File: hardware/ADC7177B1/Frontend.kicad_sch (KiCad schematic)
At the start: 55 parts, among them J4 Conn_01x01, J5 Conn_01x01, J6 Conn_01x01, J7 Conn_01x01, K1 G6SK-2F-DC5, Q6 MMBT3904, Q7 MMBT3904, U12 AD8599ARZ, U13 AD8599ARZ, U14 CPC1002N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

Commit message: PCB
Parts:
- R31, R32, R33, R34, R35, R36, R37, R38, R39, R40, R41, R42: now not fitted; now left out of the parts list
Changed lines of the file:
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@@
 		(unit 1)
 		(exclude_from_sim no)
-		(in_bom yes)
+		(in_bom no)
 		(on_board yes)
-		(dnp no)
+		(dnp yes)
 		(fields_autoplaced yes)
 		(property "Reference" "R40"
@@
 		(unit 1)
 		(exclude_from_sim no)
-		(in_bom yes)
+		(in_bom no)
 		(on_board yes)
-		(dnp no)
+		(dnp yes)
 		(fields_autoplaced yes)
 		(property "Reference" "R33"
@@
 		(unit 1)
 		(exclude_from_sim no)
-		(in_bom yes)
+		(in_bom no)
 		(on_board yes)
-		(dnp no)
+		(dnp yes)
 		(fields_autoplaced yes)
 		(property "Reference" "R38"
@@
 		(unit 1)
 		(exclude_from_sim no)
-		(in_bom yes)
+		(in_bom no)
 		(on_board yes)
-		(dnp no)
+		(dnp yes)
 		(fields_autoplaced yes)
 		(property "Reference" "R37"
@@
 		(unit 1)
 		(exclude_from_sim no)
-		(in_bom yes)
+		(in_bom no)
 		(on_board yes)
-		(dnp no)
+		(dnp yes)
 		(fields_autoplaced yes)
 		(property "Reference" "R34"
@@
 		(unit 1)
 		(exclude_from_sim no)
-		(in_bom yes)
+		(in_bom no)
 		(on_board yes)
-		(dnp no)
+		(dnp yes)
 		(fields_autoplaced yes)
 		(property "Reference" "R36"
@@
 		(unit 1)
 		(exclude_from_sim no)
-		(in_bom yes)
+		(in_bom no)
 		(on_board yes)
-		(dnp no)
+		(dnp yes)
 		(fields_autoplaced yes)
 		(property "Reference" "R31"
@@
 		(unit 1)
 		(exclude_from_sim no)
-		(in_bom yes)
+		(in_bom no)
 		(on_board yes)
-		(dnp no)
+		(dnp yes)
 		(fields_autoplaced yes)
 		(property "Reference" "R42"
@@
 		(unit 1)
 		(exclude_from_sim no)
-		(in_bom yes)
+		(in_bom no)
 		(on_board yes)
-		(dnp no)
+		(dnp yes)
 		(fields_autoplaced yes)
 		(property "Reference" "R39"
@@
 		(unit 1)
 		(exclude_from_sim no)
-		(in_bom yes)
+		(in_bom no)
 		(on_board yes)
-		(dnp no)
+		(dnp yes)
 		(fields_autoplaced yes)
 		(property "Reference" "R32"
@@
 		(unit 1)
 		(exclude_from_sim no)
-		(in_bom yes)
+		(in_bom no)
 		(on_board yes)
-		(dnp no)
+		(dnp yes)
 		(fields_autoplaced yes)
 		(property "Reference" "R35"
@@
 		(unit 1)
 		(exclude_from_sim no)
-		(in_bom yes)
+		(in_bom no)
 		(on_board yes)
-		(dnp no)
+		(dnp yes)
 		(fields_autoplaced yes)
 		(property "Reference" "R41"

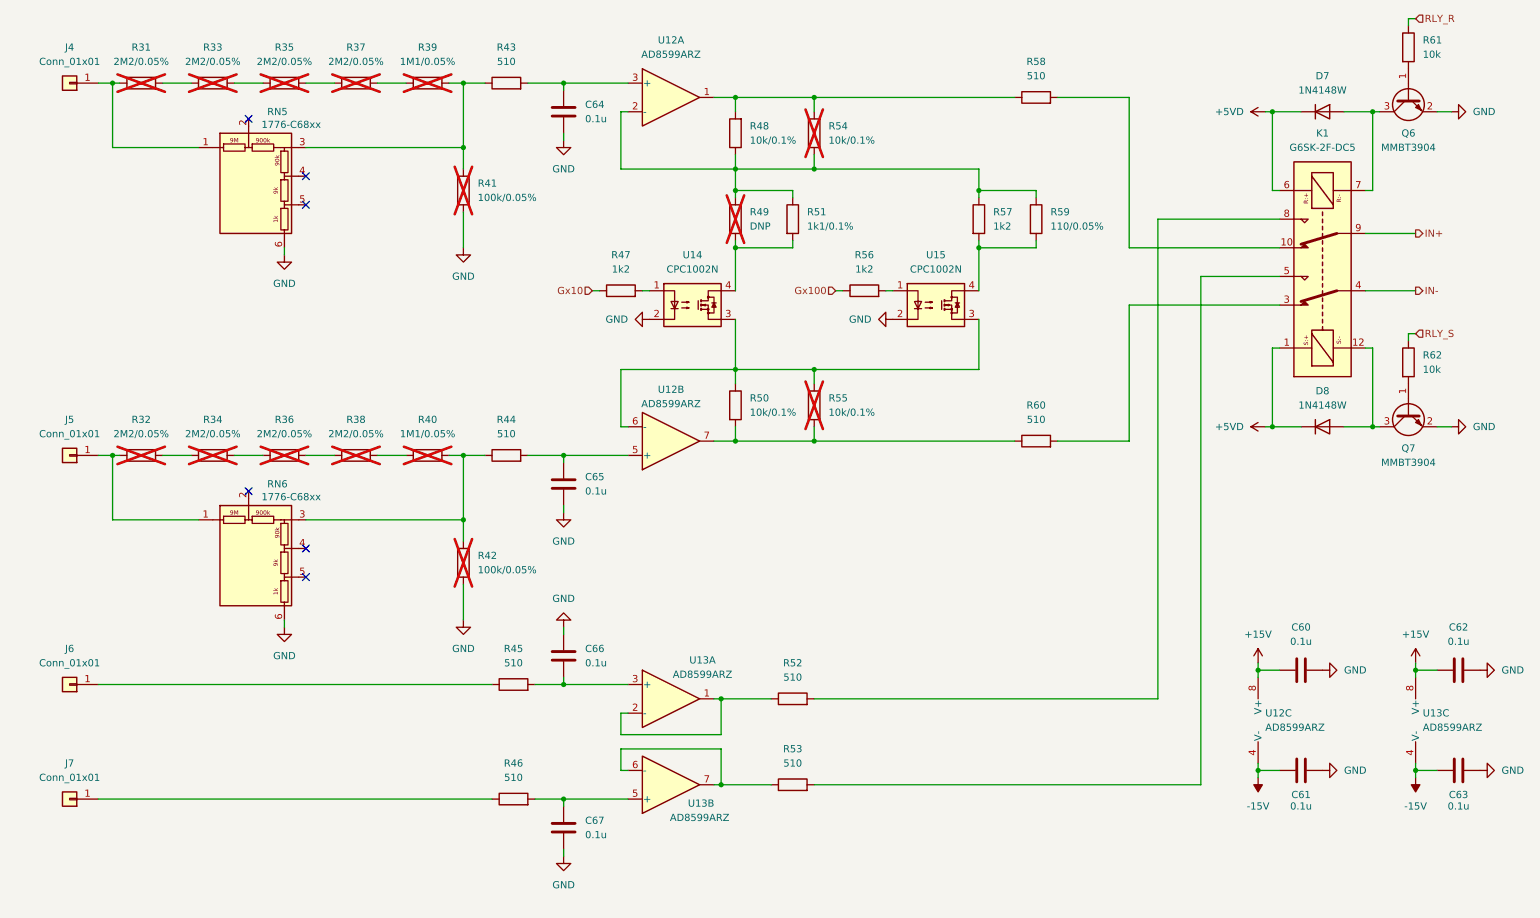
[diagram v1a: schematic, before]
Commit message: Schematic changes
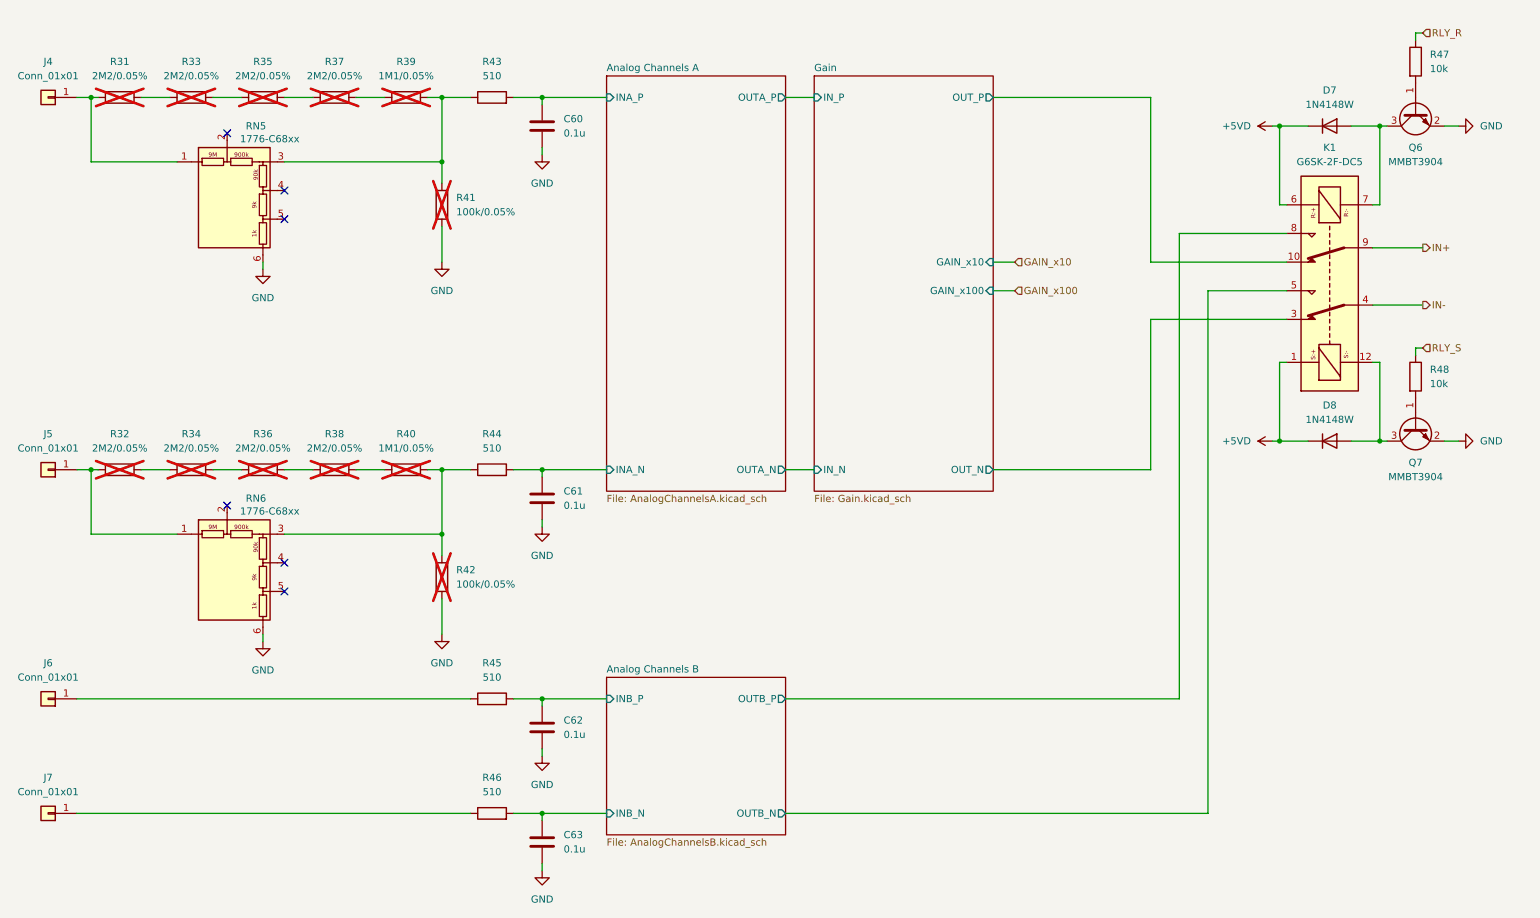
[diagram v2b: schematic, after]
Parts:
- removed C60, C61, C62, C63: 0.1u, Capacitor_SMD:C_0603_1608Metric_Pad1.08x0.95mm_HandSolder, symbol Device:C
- removed R47, R56, R57: 1k2, Resistor_SMD:R_0603_1608Metric_Pad0.98x0.95mm_HandSolder, symbol Device:R
- removed R48, R50, R54, R55: 10k/0.1%, Resistor_SMD:R_0603_1608Metric_Pad0.98x0.95mm_HandSolder, symbol Device:R
- removed R49: DNP, Resistor_SMD:R_0603_1608Metric_Pad0.98x0.95mm_HandSolder, symbol Device:R
- removed R51: 1k1/0.1%, Resistor_SMD:R_0603_1608Metric_Pad0.98x0.95mm_HandSolder, symbol Device:R
- removed R52, R53, R58, R60: 510, Resistor_SMD:R_0603_1608Metric_Pad0.98x0.95mm_HandSolder, symbol Device:R
- removed R59: 110/0.05%, Resistor_SMD:R_0603_1608Metric_Pad0.98x0.95mm_HandSolder, symbol Device:R
- removed U12, U13: AD8599ARZ, Package_SO:SOIC-8_3.9x4.9mm_P1.27mm, symbol ADC7177B1:AD8599ARZ
- removed U14, U15: CPC1002N, Package_SO:SOP-4_3.8x4.1mm_P2.54mm, symbol Relay_SolidState:CPC1002N
- C60: renamed from C64; footprint Capacitor_SMD:C_0603_1608Metric_Pad1.08x0.95mm_HandSolder -> Capacitor_SMD:C_0603_1608Metric
- C61: renamed from C65; footprint Capacitor_SMD:C_0603_1608Metric_Pad1.08x0.95mm_HandSolder -> Capacitor_SMD:C_0603_1608Metric
- C62: renamed from C66; footprint Capacitor_SMD:C_0603_1608Metric_Pad1.08x0.95mm_HandSolder -> Capacitor_SMD:C_0603_1608Metric
- C63: renamed from C67; footprint Capacitor_SMD:C_0603_1608Metric_Pad1.08x0.95mm_HandSolder -> Capacitor_SMD:C_0603_1608Metric
- renumbered R61 to R47, R62 to R48
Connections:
- net GND: now also C62.1; no longer C62.2
- net Analog Channels A/INA_N: now reaches C61.2, R44.2
- net Analog Channels A/INA_P: now reaches C60.2, R43.2
- net Analog Channels B/INB_P: now reaches R45.2
- net Analog Channels B/INB_P: now also C62.2; no longer C62.1
- net Gain/OUT_P: now reaches K1.10
- net Analog Channels B/INB_N: now reaches C63.2, R46.2
- net Gain/OUT_N: now reaches K1.3
- net Analog Channels B/OUTB_N: now reaches K1.5
- net Analog Channels B/OUTB_P: now reaches K1.8
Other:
- added sheet Analog Channels A (AnalogChannelsA.kicad_sch)
- added sheet Analog Channels B (AnalogChannelsB.kicad_sch)
- added sheet Gain (Gain.kicad_sch)
- moved on the sheet: C60, C61, C62, C63, D7, D8, J4, J5, J6, J7, K1, Q6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
